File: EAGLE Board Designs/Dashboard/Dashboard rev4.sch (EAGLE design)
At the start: 95 parts, among them J1 CONNECTOR-AVR-ISP_2X05_SMD, J2 CONNECTOR-6_μF_S_RA_, J3 CONNECTOR-CAN_μF_S_RA_, J4 CONNECTOR-8_μF_S_RA_, J5 JUMPER_0603_, Q1 TRANSISTOR_N_MOS__PMV15ENEA, Q2 TRANSISTOR_N_MOS__PMV15ENEA, Q3 TRANSISTOR_N_MOS__PMV15ENEA, Q4 TRANSISTOR_N_MOS__PMV15ENEA, Q5 TRANSISTOR_N_MOS__PMV15ENEA, Q6 TRANSISTOR_N_MOS__PMV15ENEA, Q7 TRANSISTOR_N_MOS__PMV15ENEA, U1 ATMEGA328P-AU, U2 RE46C100, U3 MCP23S08, U4 MCP2562FD, U5 MCP2515, X1 CRYSTAL_16MHZ, X2 CRYSTAL_16MHZ

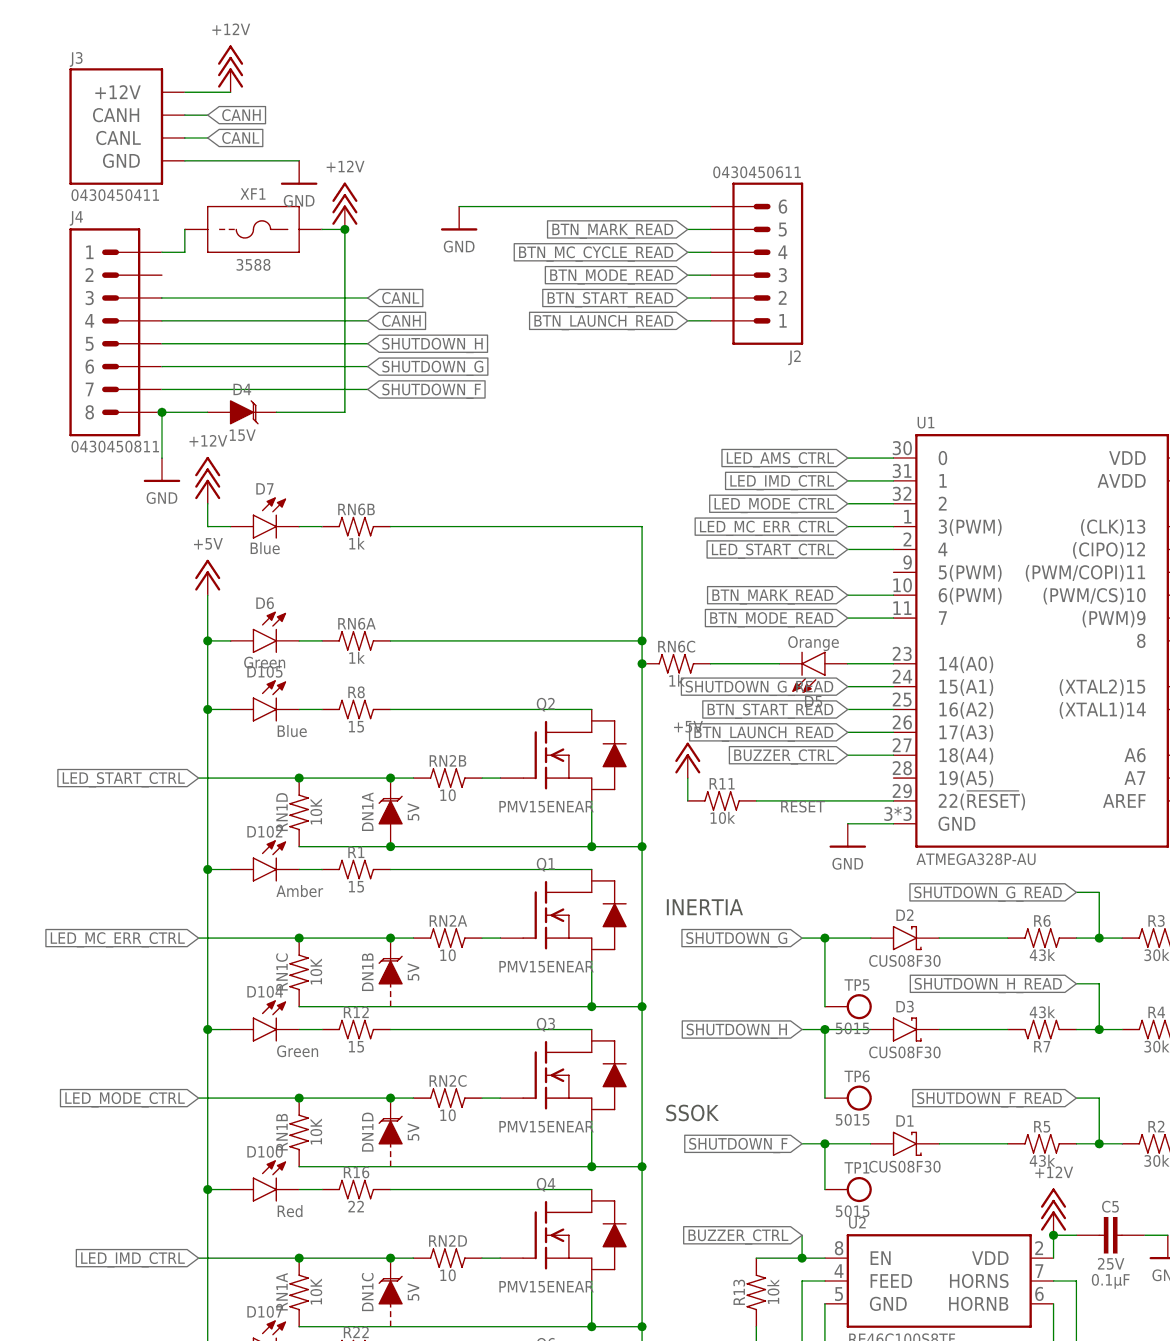
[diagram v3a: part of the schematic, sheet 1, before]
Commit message: Removed shutdown circuitry diodes
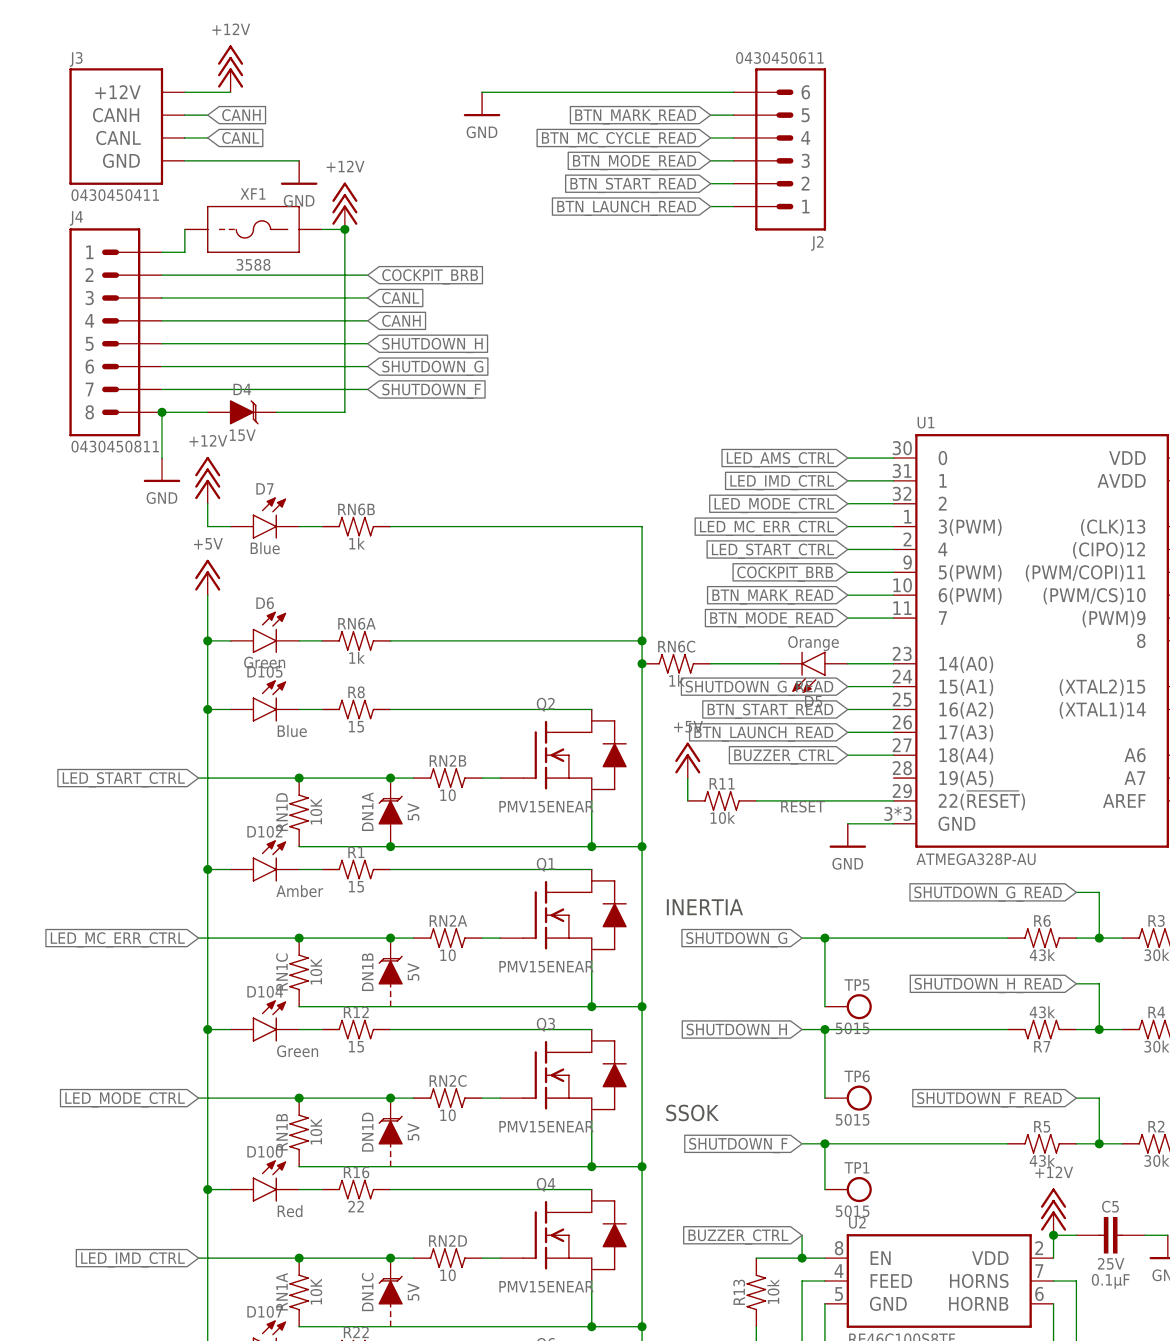
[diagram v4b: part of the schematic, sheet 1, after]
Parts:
- removed D1, D2, D3: SCHOTTKY_SOD323_30V, HyTechDevices:SCHOTTKY_SOD323_30V
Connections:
- removed net N$32: D1.C, R5.1
- removed net N$33: D3.C, R7.1
- removed net N$69: D2.C, R6.1
- new net COCKPIT_BRB: J4.2
- new net N$58: U1.5(PWM)
- net SHUTDOWN_F: now also R5.1; no longer D1.A
- net SHUTDOWN_G: now also R6.1; no longer D2.A
- net SHUTDOWN_H: now also R7.1; no longer D3.A
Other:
- moved on the sheet: J2
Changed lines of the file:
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@@
 <part name="R2" library="HyTechDevices" deviceset="RESISTOR_?_*" device="0603" technology="30K"/>
 <part name="XF1" library="HyTechDevices" deviceset="FUSE_HOLDER_*" device="SMD" technology="MINIBLADE"/>
-<part name="D2" library="HyTechDevices" deviceset="SCHOTTKY_?_*" device="SOD323" technology="30V"/>
-<part name="D3" library="HyTechDevices" deviceset="SCHOTTKY_?_*" device="SOD323" technology="30V"/>
-<part name="D1" library="HyTechDevices" deviceset="SCHOTTKY_?_*" device="SOD323" technology="30V"/>
 <part name="P25" library="HyTechSupplies" deviceset="GND" device=""/>
 <part name="FRAME2" library="HyTechFrames" deviceset="FRAME" device=""/>
@@
 <attribute name="VALUE" x="35.56" y="194.31" size="1.27" layer="96" align="top-center"/>
 </instance>
-<instance part="P18" gate="1" x="53.34" y="190.5" smashed="yes">
-<attribute name="VALUE" x="53.34" y="189.23" size="1.27" layer="96" align="top-center"/>
+<instance part="P18" gate="1" x="55.88" y="203.2" smashed="yes">
+<attribute name="VALUE" x="55.88" y="201.93" size="1.27" layer="96" align="top-center"/>
 </instance>
 <instance part="P20" gate="1" x="271.78" y="180.34" smashed="yes">
@@
 <attribute name="MPN" x="96.52" y="67.818" size="1.27" layer="96" align="top-left"/>
 </instance>
-<instance part="J2" gate="G$1" x="91.44" y="177.8" smashed="yes" rot="R180">
-<attribute name="NAME" x="91.44" y="177.038" size="1.27" layer="95" rot="R180"/>
-<attribute name="MPN" x="91.44" y="196.215" size="1.27" layer="96" rot="R180" align="top-left"/>
+<instance part="J2" gate="G$1" x="93.98" y="190.5" smashed="yes" rot="R180">
+<attribute name="NAME" x="93.98" y="189.738" size="1.27" layer="95" rot="R180"/>
+<attribute name="MPN" x="93.98" y="208.915" size="1.27" layer="96" rot="R180" align="top-left"/>
 </instance>
 <instance part="DN1" gate="E" x="45.72" y="55.88" smashed="yes" rot="R90">
@@
 <attribute name="NAME" x="30.48" y="193.802" size="1.27" layer="95" align="bottom-center"/>
 <attribute name="MPN" x="30.48" y="187.198" size="1.27" layer="96" align="top-center"/>
-</instance>
-<instance part="D2" gate="G$1" x="104.14" y="111.76" smashed="yes">
-<attribute name="NAME" x="102.87" y="113.665" size="1.27" layer="95" align="bottom-center"/>
-<attribute name="MPN" x="102.87" y="109.855" size="1.27" layer="96" align="top-center"/>
-</instance>
-<instance part="D3" gate="G$1" x="104.14" y="101.6" smashed="yes">
-<attribute name="NAME" x="102.87" y="103.505" size="1.27" layer="95" align="bottom-center"/>
-<attribute name="MPN" x="102.87" y="99.695" size="1.27" layer="96" align="top-center"/>
-</instance>
-<instance part="D1" gate="G$1" x="104.14" y="88.9" smashed="yes">
-<attribute name="NAME" x="102.87" y="90.805" size="1.27" layer="95" align="bottom-center"/>
-<attribute name="MPN" x="102.87" y="86.995" size="1.27" layer="96" align="top-center"/>
 </instance>
 <instance part="P25" gate="1" x="236.22" y="182.88" smashed="yes">
@@
 </segment>
 <segment>
-<wire x1="81.28" y1="193.04" x2="53.34" y2="193.04" width="0.1524" layer="91"/>
+<wire x1="83.82" y1="205.74" x2="55.88" y2="205.74" width="0.1524" layer="91"/>
 <pinref part="P18" gate="1" pin="GND"/>
 <pinref part="J2" gate="G$1" pin="6"/>
@@
 <net name="BTN_MARK_READ" class="0">
 <segment>
-<wire x1="81.28" y1="190.5" x2="78.74" y2="190.5" width="0.1524" layer="91"/>
-<label x="78.74" y="190.5" size="1.27" layer="95" rot="R180" xref="yes"/>
+<wire x1="83.82" y1="203.2" x2="81.28" y2="203.2" width="0.1524" layer="91"/>
+<label x="81.28" y="203.2" size="1.27" layer="95" rot="R180" xref="yes"/>
 <pinref part="J2" gate="G$1" pin="5"/>
 </segment>
@@
 <net name="BTN_MODE_READ" class="0">
 <segment>
-<wire x1="81.28" y1="185.42" x2="78.74" y2="185.42" width="0.1524" layer="91"/>
-<label x="78.74" y="185.42" size="1.27" layer="95" rot="R180" xref="yes"/>
+<wire x1="83.82" y1="198.12" x2="81.28" y2="198.12" width="0.1524" layer="91"/>
+<label x="81.28" y="198.12" size="1.27" layer="95" rot="R180" xref="yes"/>
 <pinref part="J2" gate="G$1" pin="3"/>
 </segment>
@@
 <net name="BTN_MC_CYCLE_READ" class="0">
 <segment>
-<wire x1="81.28" y1="187.96" x2="78.74" y2="187.96" width="0.1524" layer="91"/>
-<label x="78.74" y="187.96" size="1.27" layer="95" rot="R180" xref="yes"/>
+<wire x1="83.82" y1="200.66" x2="81.28" y2="200.66" width="0.1524" layer="91"/>
+<label x="81.28" y="200.66" size="1.27" layer="95" rot="R180" xref="yes"/>
 <pinref part="J2" gate="G$1" pin="4"/>
 </segment>
@@
 </segment>
 <segment>
-<wire x1="81.28" y1="182.88" x2="78.74" y2="182.88" width="0.1524" layer="91"/>
-<label x="78.74" y="182.88" size="1.27" layer="95" rot="R180" xref="yes"/>
+<wire x1="83.82" y1="195.58" x2="81.28" y2="195.58" width="0.1524" layer="91"/>
+<label x="81.28" y="195.58" size="1.27" layer="95" rot="R180" xref="yes"/>
 <pinref part="J2" gate="G$1" pin="2"/>
 </segment>
@@
 <net name="SHUTDOWN_F" class="0">
 <segment>
-<wire x1="99.06" y1="88.9" x2="93.98" y2="88.9" width="0.1524" layer="91"/>
 <label x="91.44" y="88.9" size="1.27" layer="95" rot="R180" xref="yes"/>
-<pinref part="D1" gate="G$1" pin="A"/>
 <pinref part="TP1" gate="G$1" pin="P$1"/>
 <wire x1="93.98" y1="88.9" x2="91.44" y2="88.9" width="0.1524" layer="91"/>
 <wire x1="93.98" y1="83.82" x2="93.98" y2="88.9" width="0.1524" layer="91"/>
 <junction x="93.98" y="88.9"/>
+<pinref part="R5" gate="G$1" pin="1"/>
+<wire x1="93.98" y1="88.9" x2="114.3" y2="88.9" width="0.1524" layer="91"/>
 </segment>
 <segment>
@@
 </segment>
 <segment>
-<wire x1="81.28" y1="180.34" x2="78.74" y2="180.34" width="0.1524" layer="91"/>
-<label x="78.74" y="180.34" size="1.27" layer="95" rot="R180" xref="yes"/>
+<wire x1="83.82" y1="193.04" x2="81.28" y2="193.04" width="0.1524" layer="91"/>
+<label x="81.28" y="193.04" size="1.27" layer="95" rot="R180" xref="yes"/>
 <pinref part="J2" gate="G$1" pin="1"/>
 </segment>
@@
 <net name="SHUTDOWN_H" class="0">
 <segment>
-<wire x1="99.06" y1="101.6" x2="93.98" y2="101.6" width="0.1524" layer="91"/>
 <label x="91.44" y="101.6" size="1.27" layer="95" rot="R180" xref="yes"/>
-<pinref part="D3" gate="G$1" pin="A"/>
 <pinref part="TP6" gate="G$1" pin="P$1"/>
 <wire x1="93.98" y1="101.6" x2="91.44" y2="101.6" width="0.1524" layer="91"/>
 <wire x1="93.98" y1="93.98" x2="93.98" y2="101.6" width="0.1524" layer="91"/>
 <junction x="93.98" y="101.6"/>
+<pinref part="R7" gate="G$1" pin="1"/>
+<wire x1="93.98" y1="101.6" x2="114.3" y2="101.6" width="0.1524" layer="91"/>
 </segment>
 <segment>
@@
 <pinref part="D105" gate="LED" pin="C"/>
 <pinref part="R8" gate="G$1" pin="1"/>
-</segment>
-</net>
-<net name="N$32" class="0">
-<segment>
-<wire x1="106.68" y1="88.9" x2="114.3" y2="88.9" width="0.1524" layer="91"/>
-<pinref part="R5" gate="G$1" pin="1"/>
-<pinref part="D1" gate="G$1" pin="C"/>
-</segment>
-</net>
-<net name="N$33" class="0">
-<segment>
-<wire x1="106.68" y1="101.6" x2="114.3" y2="101.6" width="0.1524" layer="91"/>
-<pinref part="R7" gate="G$1" pin="1"/>
-<pinref part="D3" gate="G$1" pin="C"/>
 </segment>
 </net>
@@
 </segment>
 </net>
-<net name="N$69" class="0">
-<segment>
-<wire x1="106.68" y1="111.76" x2="114.3" y2="111.76" width="0.1524" layer="91"/>
-<pinref part="R6" gate="G$1" pin="1"/>
-<pinref part="D2" gate="G$1" pin="C"/>
-</segment>
-</net>
 <net name="SHUTDOWN_G" class="0">
 <segment>
-<wire x1="99.06" y1="111.76" x2="93.98" y2="111.76" width="0.1524" layer="91"/>
 <label x="91.44" y="111.76" size="1.27" layer="95" rot="R180" xref="yes"/>
-<pinref part="D2" gate="G$1" pin="A"/>
 <pinref part="TP5" gate="G$1" pin="P$1"/>
 <wire x1="93.98" y1="111.76" x2="91.44" y2="111.76" width="0.1524" layer="91"/>
 <wire x1="93.98" y1="104.14" x2="93.98" y2="111.76" width="0.1524" layer="91"/>
 <junction x="93.98" y="111.76"/>
+<pinref part="R6" gate="G$1" pin="1"/>
+<wire x1="93.98" y1="111.76" x2="114.3" y2="111.76" width="0.1524" layer="91"/>
 </segment>
 <segment>
@@
 </segment>
 </net>
+<net name="COCKPIT_BRB" class="0">
+<segment>
+<pinref part="J4" gate="G$1" pin="2"/>
+<wire x1="20.32" y1="185.42" x2="43.18" y2="185.42" width="0.1524" layer="91"/>
+<label x="43.18" y="185.42" size="1.27" layer="95" xref="yes"/>
+<label x="96.52" y="152.4" size="1.27" layer="95" rot="R180" xref="yes"/>
+</segment>
+</net>
+<net name="N$58" class="0">
+<segment>
+<pinref part="U1" gate="G$1" pin="5(PWM)"/>
+<wire x1="101.6" y1="152.4" x2="96.52" y2="152.4" width="0.1524" layer="91"/>
+</segment>
+</net>

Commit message: Cleanup up routing and test points
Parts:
- removed RN3: RESISTOR_NETWORK_4_100, HyTechDevices:RESISTOR_NETWORK_4_100
- added D1: LED_2835_AMBER, HyTechDevices:LED_2835_AMBER
- added Q8: TRANSISTOR_N_MOS__PMV15ENEA, HyTechDevices:TRANSISTOR_N_MOS__PMV15ENEA
- added R23: RESISTOR_0603_15, HyTechDevices:RESISTOR_0603_15
- added R24: RESISTOR_0603_43K, HyTechDevices:RESISTOR_0603_43K
- added R25: RESISTOR_0603_30K, HyTechDevices:RESISTOR_0603_30K
- added TP7: TEST_POINT, HyTechDevices:TEST_POINT
- TP1: SIGNAL SSOK -> SHUTDOWN_F
- TP5: SIGNAL SSOK -> SHUTDOWN_G
- TP6: SIGNAL SSOK -> SHUTDOWN_H
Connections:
- net N$59 renamed CS_IO
- removed net N$45: RN3A.1, U1.(CLK)13
- removed net N$47: RN3B.1, U1.(CIPO)12
- removed net N$48: RN3C.1, U1.(PWM/COPI)11
- removed net N$56: J1.COPI, RN3C.2, U3.SDI, U5.SDI
- removed net N$57: RN3D.2, U5.!CS
- removed net N$58: U1.5(PWM)
- new net CIPO: J1.CIPO, U1.(CIPO)12, U3.SDO, U5.SDO
- new net CLK: J1.CLK, U1.(CLK)13, U3.CLK, U5.CLK
- new net COCKPIT_BRB_READ: DN2C.C, R24.2, R25.1, RN4D.2, RN8D.1, U1.5(PWM)
- new net COPI: J1.COPI, U1.(PWM/COPI)11, U3.SDI, U5.SDI
- new net CS_CAN: U1.(PWM/CS)10, U5.!CS
- net +12V: now also TP2.1; no longer TP2.P$1
- net +5V: now also D1.A, TP3.1; no longer TP3.P$1
- net COCKPIT_BRB: now also R24.1, TP7.1
- net GND: now also Q8.S, R25.2, RN4D.1, TP4.1; no longer TP4.P$1
- net N$12: now also Q8.G, RN8D.2; no longer J1.CLK, RN3A.2, U3.CLK, U5.CLK
- net N$20: now also D1.C, R23.1; no longer RN3D.1, U1.(PWM/CS)10
- net N$23: now also Q8.D, R23.2; no longer J1.CIPO, RN3B.2, U3.SDO, U5.SDO
- net SHUTDOWN_F: now also TP1.1; no longer TP1.P$1
- net SHUTDOWN_G: now also TP5.1; no longer TP5.P$1
- net SHUTDOWN_H: now also TP6.1; no longer TP6.P$1
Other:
- note added: "Schematic of Dashboard PCB for HT05 : Error and State LEDs"
- note added: "Schematic of Dashboard PCB for HT05 : Microcontroller, CAN, 7-Segment Display Connectors"
- note added: "Schematic of Dashboard PCB for HT05 : Shutdown and Buzzer Control Circuitry"
- note removed: "Schematic of the Dashboard PCB for HT05"
